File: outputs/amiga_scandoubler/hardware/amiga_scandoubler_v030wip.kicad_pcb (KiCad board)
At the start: 4 copper layers, 95 x 95 mm, 139 parts, among them J1 33DSMT1-E15SNCT, J2 33DSMT1-E15SNCT, J3 TYPE-C-31-M-12, J4 JTAG 2x05 2.54mm, U1 TVP7002PZP, U2 GW1N-LV4QN88C6/I5, U3 ADV7125KSTZ140, U4 SN74LVC2G17DBVR, U5 SN74LVC2G17DBVR, U6 SN74LVC1G17DBVR, U7 TPS62160DSGR, U8 TPS62160DSGR, U9 TPS62160DSGR, Y1 27MHz ECS-3225MVLC

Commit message: Replace Y1 with YXC OT2EL4C4JI-111OLP-27M; reselect parts for 2 boards
- Y1: ECS-3225MVLC-270 (LCSC stock 4) -> C5203549, a pin/land-compatible 3225 CMOS oscillator (datasheet checked). Footprint and routing unchanged.
- Selection re-run for a 2-board build (JLCPCB PCBA minimum is 2). U1 is covered (stock 4). J1/J2 carry C3146802 for Global Sourcing.
- All 139 parts now have LCSC numbers.
- Nets still match (595 nodes). DRC errors 0, unconnected 0. The audit passes.

Co-Authored-By: Claude Opus 5.5 <noreply@anthropic.com>
Claude-Session: https://claude.ai/code/session_019f929sAJ7LRnJRRFvA6g9F
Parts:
- Y1: value 27MHz ECS-3225MVLC -> 27MHz OT2EL4C4JI-111OLP-27M
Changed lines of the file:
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@@
         (effects (font (size 0.8 0.8) (thickness 0.15)))
     )
-    (fp_text value "27MHz ECS-3225MVLC" (at 0 6) (layer "F.Fab") hide
+    (fp_text value "27MHz OT2EL4C4JI-111OLP-27M" (at 0 6) (layer "F.Fab") hide
         (effects (font (size 0.8 0.8) (thickness 0.1)))
     )

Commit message: Replace J1/J2 with THT HYC06-HDR15B-060 (3-row DE-15 female)
- New footprint DE15_HOAUC_HYC06-HDR15B-060 from the HOAUC drawing
  (rows 3.08/5.06/7.04 mm from edge, 2.29x1.98 pitch, 2x 3.2 mm PTH locks).
- Board: old CONEC SMD footprints and their fan-out removed (jc_rm.py),
  new parts placed (jc_add.py), 10 signals re-routed with router7 (3 vias),
  covered references re-placed (jc_silk.py).
- DRC 0 errors / 0 unconnected, audit PASS, schematic netlist matches
  (570 connected nodes), drill hits match.
- Schematic, netlist, manifest, parts selection (C711364) and all fab
  outputs regenerated; README/revision/CLAUDE.md updated.

Co-Authored-By: Claude Opus 5.5 <noreply@anthropic.com>
Claude-Session: https://claude.ai/code/session_019f929sAJ7LRnJRRFvA6g9F
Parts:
- J1, J2: value 33DSMT1-E15SNCT -> HYC06-HDR15B-060; footprint Amiga:DE15_Conec_33DSMT1-E15SNCT -> Amiga:DE15_HOAUC_HYC06-HDR15B-060
- moved J2 0.06 mm to (89.9, 42.0)
- moved J1 0.06 mm to (5.06, 42.0)
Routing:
- net G_OUT: track 27.0 -> 16.7 mm
- net B_OUT: track 29.3 -> 19.2 mm
- net V_IN: track 19.0 -> 28.9 mm, vias 2 -> 0
- net H_OUT: track 9.06 -> 17.7 mm, vias 2 -> 1
- net GND: track 372.5 -> 364.6 mm, vias 129 -> 120
- net V_OUT: track 20.6 -> 14.6 mm
- net R_OUT: track 22.0 -> 16.9 mm
- net G_IN: track 12.4 -> 7.68 mm, vias 0 -> 1
- net R_IN: track 10.0 -> 14.4 mm
- net B_IN: track 16.3 -> 15.7 mm, vias 0 -> 1

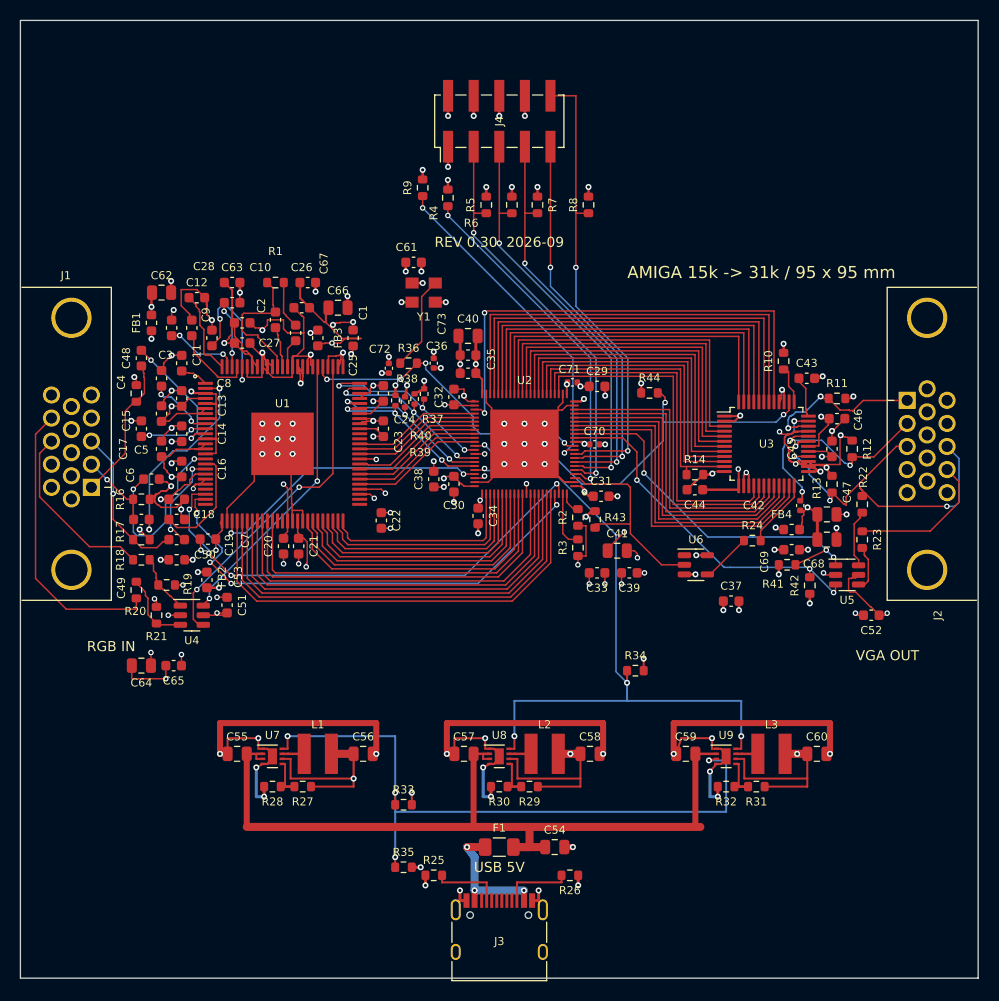
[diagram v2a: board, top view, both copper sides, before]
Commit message: JLC DFM/order fixes: move vias off pads, widen J3 slots, re-place silk, replace L1-L3, merge C15850 BOM line
- dfm_vias.py: 31 vias moved (pad gap >= 0.15 mm), via-in-pad removed on C56/C58/C59/C60/C71
- dfm_fix2.py: C71/C29 +0.4 mm, J3 footprint with 0.8 mm slots, C15850 values unified
- dfm_silk.py: 50 reference texts re-placed away from pads/holes
- L1-L3 -> Taiyo Yuden NRS4018T2R2MDGJ (C92959, EasyEDA footprint available)
- DRC 0 errors / 0 unconnected, audit PASS, ERC clean, fab outputs regenerated

Co-Authored-By: Claude Opus 5.5 <noreply@anthropic.com>
Claude-Session: https://claude.ai/code/session_019f929sAJ7LRnJRRFvA6g9F
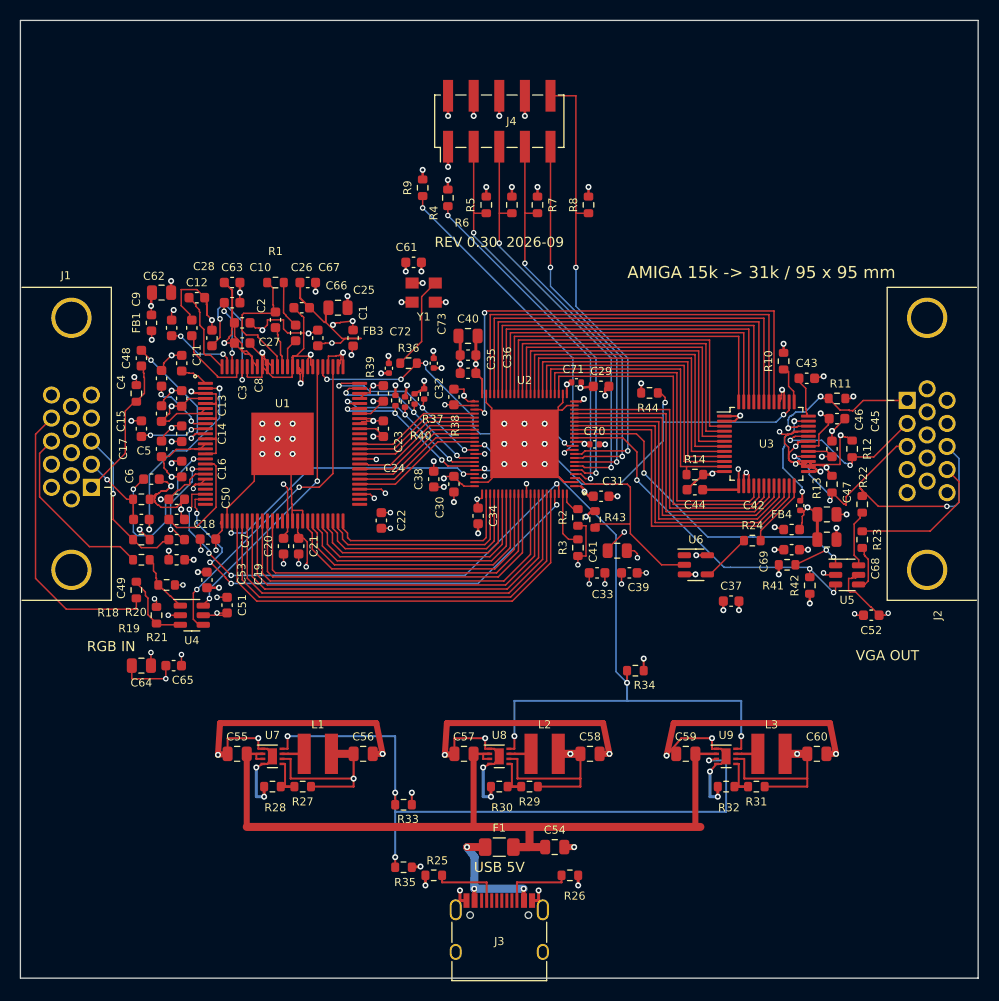
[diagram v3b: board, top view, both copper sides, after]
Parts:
- C47, C54: value 10uF -> 10uF 25V
- C55, C57, C59: value 10uF 10V -> 10uF 25V
- J3: footprint Connector_USB:USB_C_Receptacle_HRO_TYPE-C-31-M-12 -> Amiga:USB_C_Receptacle_HRO_TYPE-C-31-M-12_Slot0.8
- moved C29 0.40 mm to (57.6, 36.3)
- moved C71 0.40 mm to (55.1, 35.9)
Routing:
- net GND: track 364.6 -> 368.8 mm
- net 1V9: track 103.8 -> 102.6 mm
- net 3V3: track 84.9 -> 85.9 mm

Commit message: Fix C59 GND stub collapse from the DFM via move; square up regulator loops; add pad-connection check
- dfm_vias.py: via->pad stubs stay, untouched pads get a new track to the moved via, tiny in-via pieces deleted
- dfm_fix2.py: slanted wide legs squared back to vertical
- tools/padconn_cmp.py: no pad lost or narrowed its connection vs the pre-DFM board
- DRC 0/0, audit PASS, netlist/ERC unchanged; fab outputs regenerated

Co-Authored-By: Claude Opus 5.5 <noreply@anthropic.com>
Claude-Session: https://claude.ai/code/session_019f929sAJ7LRnJRRFvA6g9F
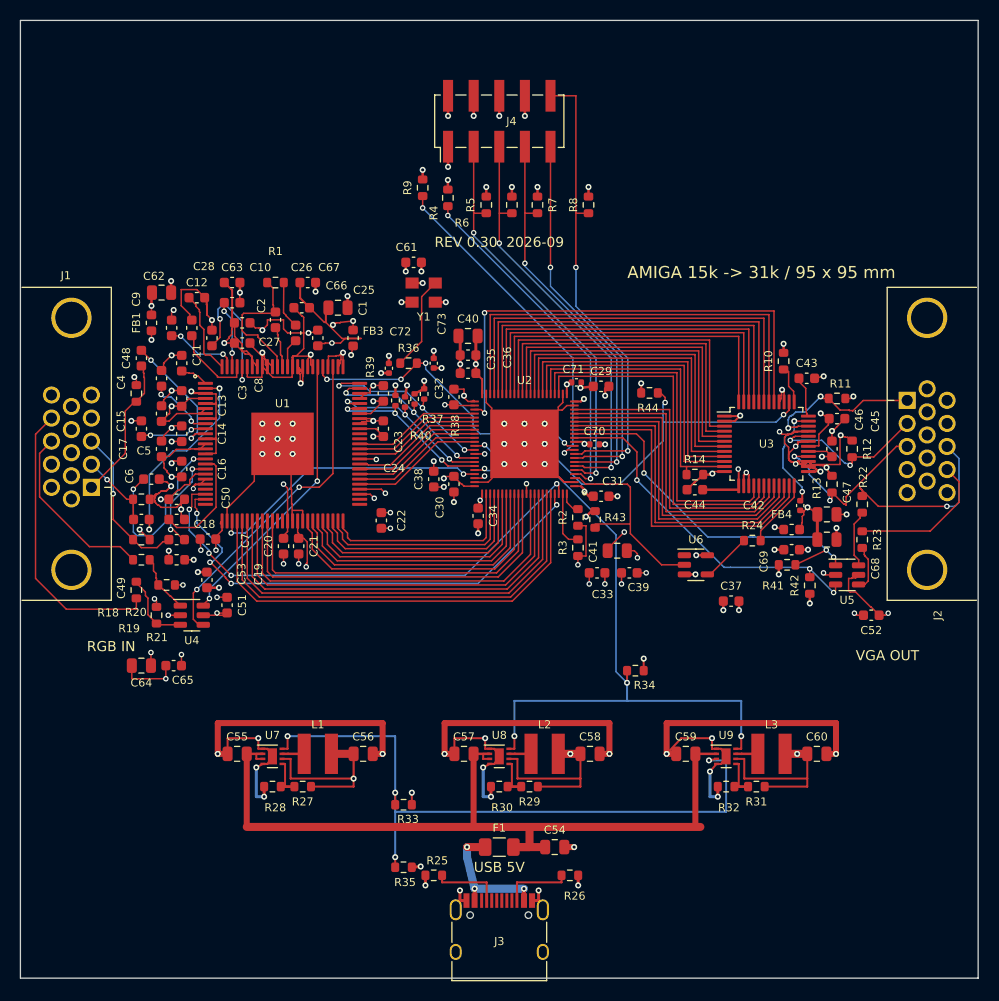
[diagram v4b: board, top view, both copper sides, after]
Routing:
- net GND: track 368.8 -> 372.4 mm

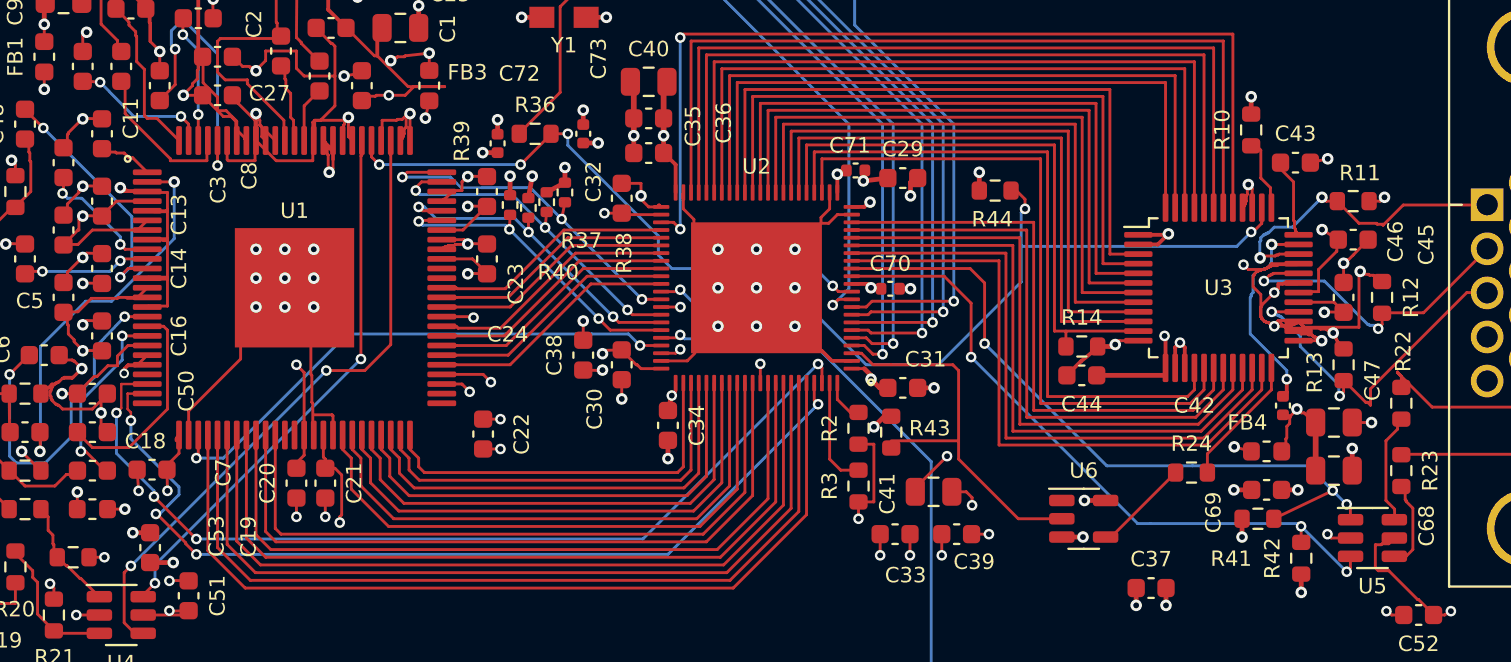
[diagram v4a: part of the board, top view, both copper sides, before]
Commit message: Remove tracks running between adjacent IC pins (U1 x11, U3 x3, U5.5); re-route the isolated pins
- dfm_u1pll.py: U1.85 straight off its tip to the ADC_1V9PLL via (JLC DFM danger 0.05 mm)
- dfm_gapfix.py: 52 gap segments + 18 dangling pieces removed, 12 pins re-routed with pin gaps blocked
- tracks in pin gaps 0, DRC 0/0, audit PASS, netlist match, no pad lost/narrowed its connection
- fab outputs regenerated (BOM/CPL unchanged)

Co-Authored-By: Claude Opus 5.5 <noreply@anthropic.com>
Claude-Session: https://claude.ai/code/session_019f929sAJ7LRnJRRFvA6g9F
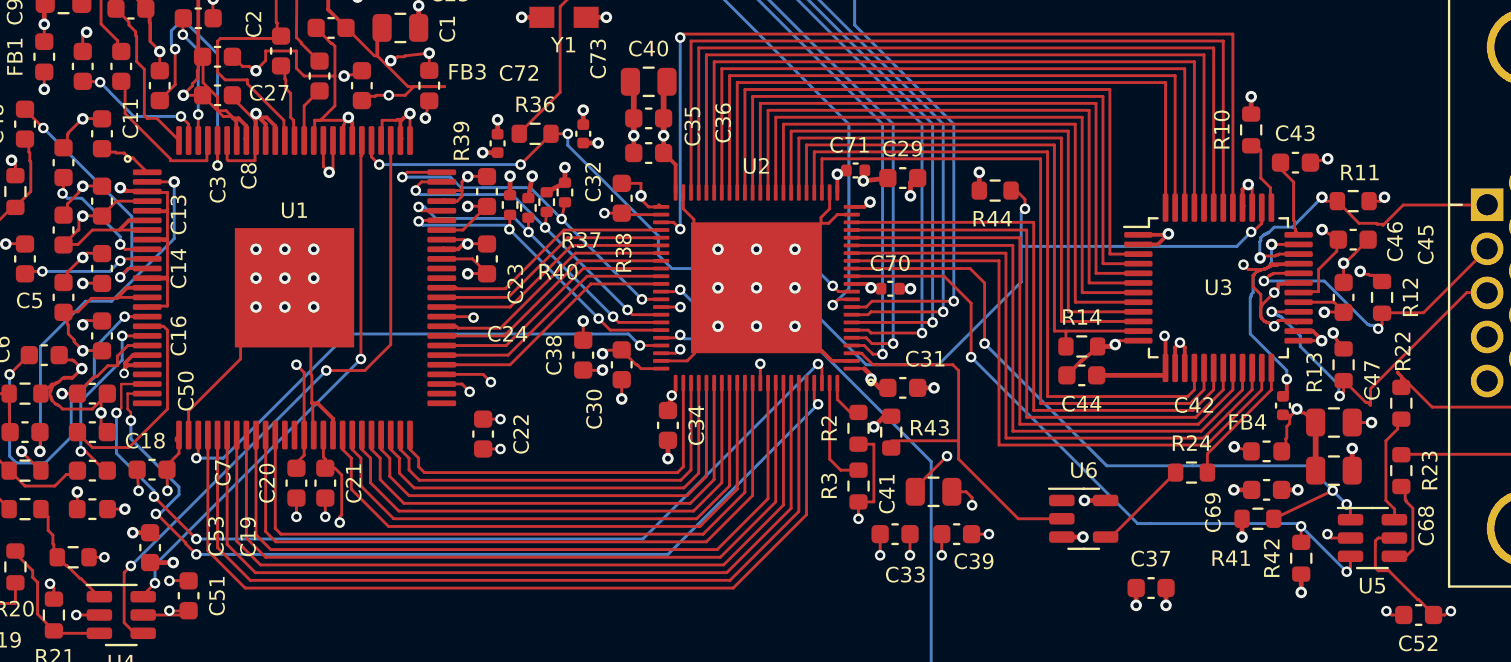
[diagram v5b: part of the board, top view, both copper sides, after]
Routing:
- net GND: track 372.4 -> 358.5 mm
- net ADC_3V3A: track 53.6 -> 55.2 mm
- net ADC_1V9PLL: track 43.2 -> 42.0 mm
- net ADC_1V9A: track 59.9 -> 60.9 mm

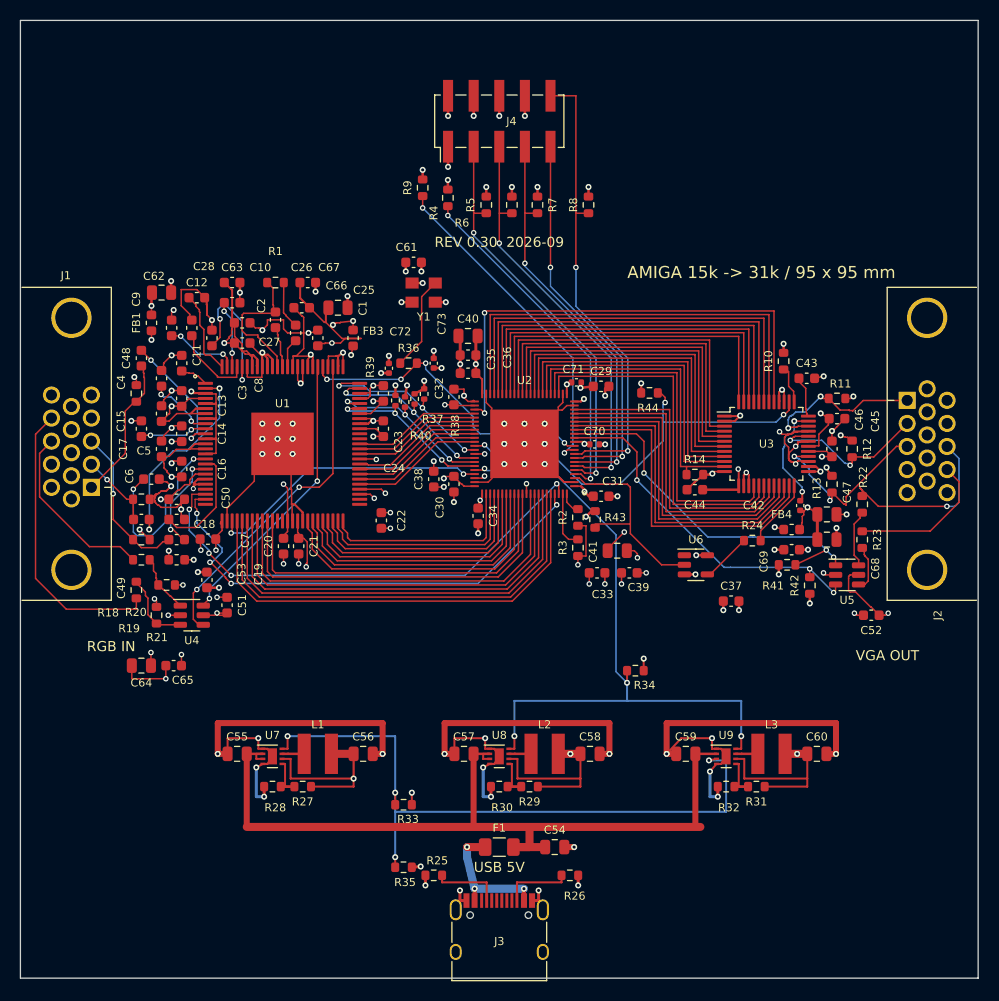
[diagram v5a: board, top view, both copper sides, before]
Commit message: Remove overlapping same-net track copies and dead spurs; tidy U1.93/94-C27/C28
- dfm_dedup.py: 44 overlapping same-net pairs -> 0 (41 copies + 9 dangling pieces, 50 lines),
  only where the net's pad connectivity is unchanged
- dfm_spur.py: dead spurs removed via biconnected blocks (ADC_1V9PLL In2 ~3 mm hairpin, H_OUT)
- dfm_tidy.py: U1.93 joins U1.94's corner, C27/C28 fed as a tree from the In2 via,
  leftover ADC_1V9PLL diagonal and H_OUT overshoot removed
- DRC 0 errors / 0 unconnected / 0 dangling, audit PASS, 570-node netlist match,
  no pad lost or narrowed its connection; fab outputs regenerated (BOM/CPL unchanged)

Co-Authored-By: Claude Opus 5.5 <noreply@anthropic.com>
Claude-Session: https://claude.ai/code/session_019f929sAJ7LRnJRRFvA6g9F
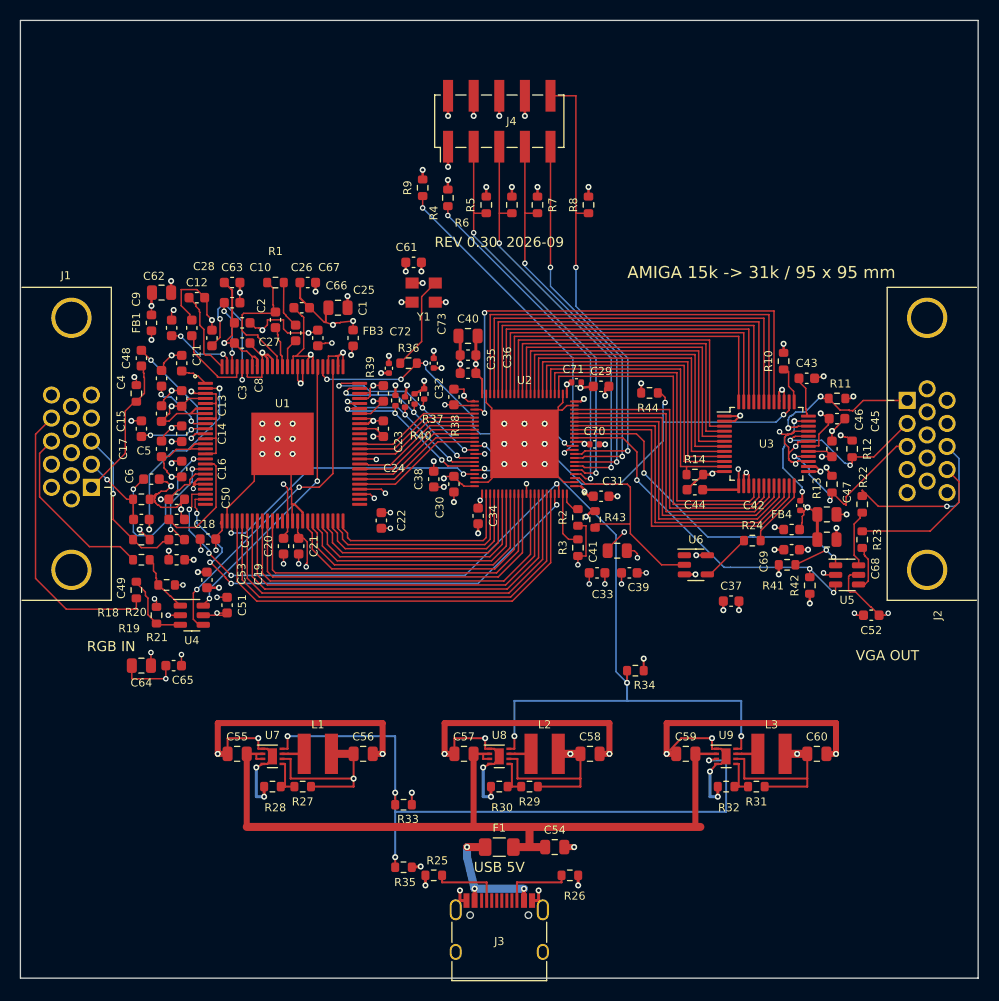
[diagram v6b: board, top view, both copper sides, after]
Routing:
- net ADC_1V9PLL: track 42.0 -> 24.8 mm
- net GND: track 358.5 -> 342.7 mm
- net ADC_3V3A: track 55.2 -> 50.1 mm
- net 3V3: track 85.7 -> 82.6 mm
- net 5V: track 82.4 -> 79.5 mm
- net FB_3V3: track 4.83 -> 3.90 mm
- net FB_1V9: track 4.82 -> 3.90 mm
- net FB_1V2: track 4.82 -> 3.90 mm
- net H_OUT: track 17.7 -> 17.1 mm
